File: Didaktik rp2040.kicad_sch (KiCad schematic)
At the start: 32 parts, among them J1 Conn_01x04_MountingPin, J5 SWD, SW43 Reset, SW44 Boot, U1 XC6206PxxxMR, U2 RP2040, U3 W25Q128JVS, U4 USBLC6-2SC6, Y2 12MHz

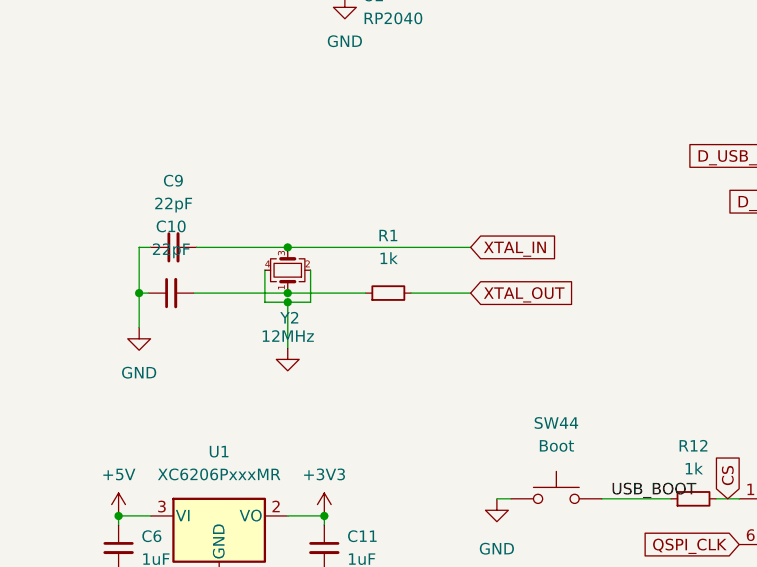
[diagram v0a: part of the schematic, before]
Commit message: MCU, component placement
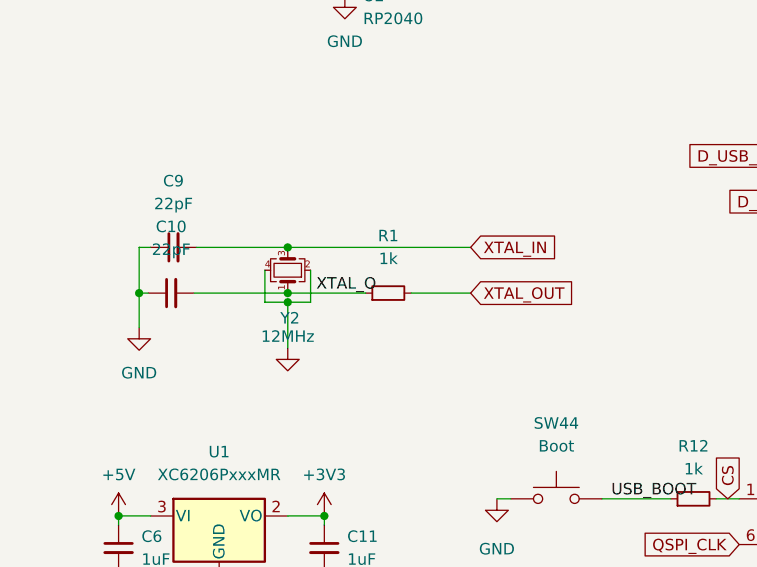
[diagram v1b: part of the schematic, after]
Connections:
- net XTAL_O: now reaches C10.2, R1.1, Y2.1
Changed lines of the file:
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@@
+    (effects (font (size 1.27 1.27)) (justify left bottom))
+  )
+  (label "XTAL_O" (at 45.72 153.035 0) (fields_autoplaced)
     (effects (font (size 1.27 1.27)) (justify left bottom))
   )

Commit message: some more cleaner MCU component placement
boot button aligned to plate cut
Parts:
- R10, R7: footprint Resistor_SMD:R_0603_1608Metric -> Resistor_SMD:R_0402_1005Metric
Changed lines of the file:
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@@
       (effects (font (size 1.27 1.27)))
     )
-    (property "Footprint" "Resistor_SMD:R_0603_1608Metric" (at 27.051 42.545 0)
+    (property "Footprint" "Resistor_SMD:R_0402_1005Metric" (at 27.051 42.545 0)
       (effects (font (size 1.27 1.27)) hide)
     )
@@
       (effects (font (size 1.27 1.27)))
     )
-    (property "Footprint" "Resistor_SMD:R_0603_1608Metric" (at 27.051 40.005 0)
-      (effects (font (size 1.27 1.27)) hide)
-    )
+    (property "Footprint" "Resistor_SMD:R_0402_1005Metric" (at 27.051 40.005 0)
+      (effects (font (size 1.27 1.27)) hide)
+    )
